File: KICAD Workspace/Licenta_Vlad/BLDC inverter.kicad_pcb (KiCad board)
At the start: 2 copper layers, 130.8 x 107.7 mm, 103 parts, among them J1 Conn_01x03, J2 Conn_01x02, J3 Conn_01x03, J4 Conn_01x02, J5 Conn_01x03, J6 Conn_01x03, Q1 BC547, Q2 IRF9530, U1 IR2101, U10 LP2950-3.3_TO92, U2 IR2101, U3 IR2101, U4 L7805, U5 LM2576HVT-12, U6 LM2576HVT-12, U7 ACS754, U8 LM393, U9 LM393

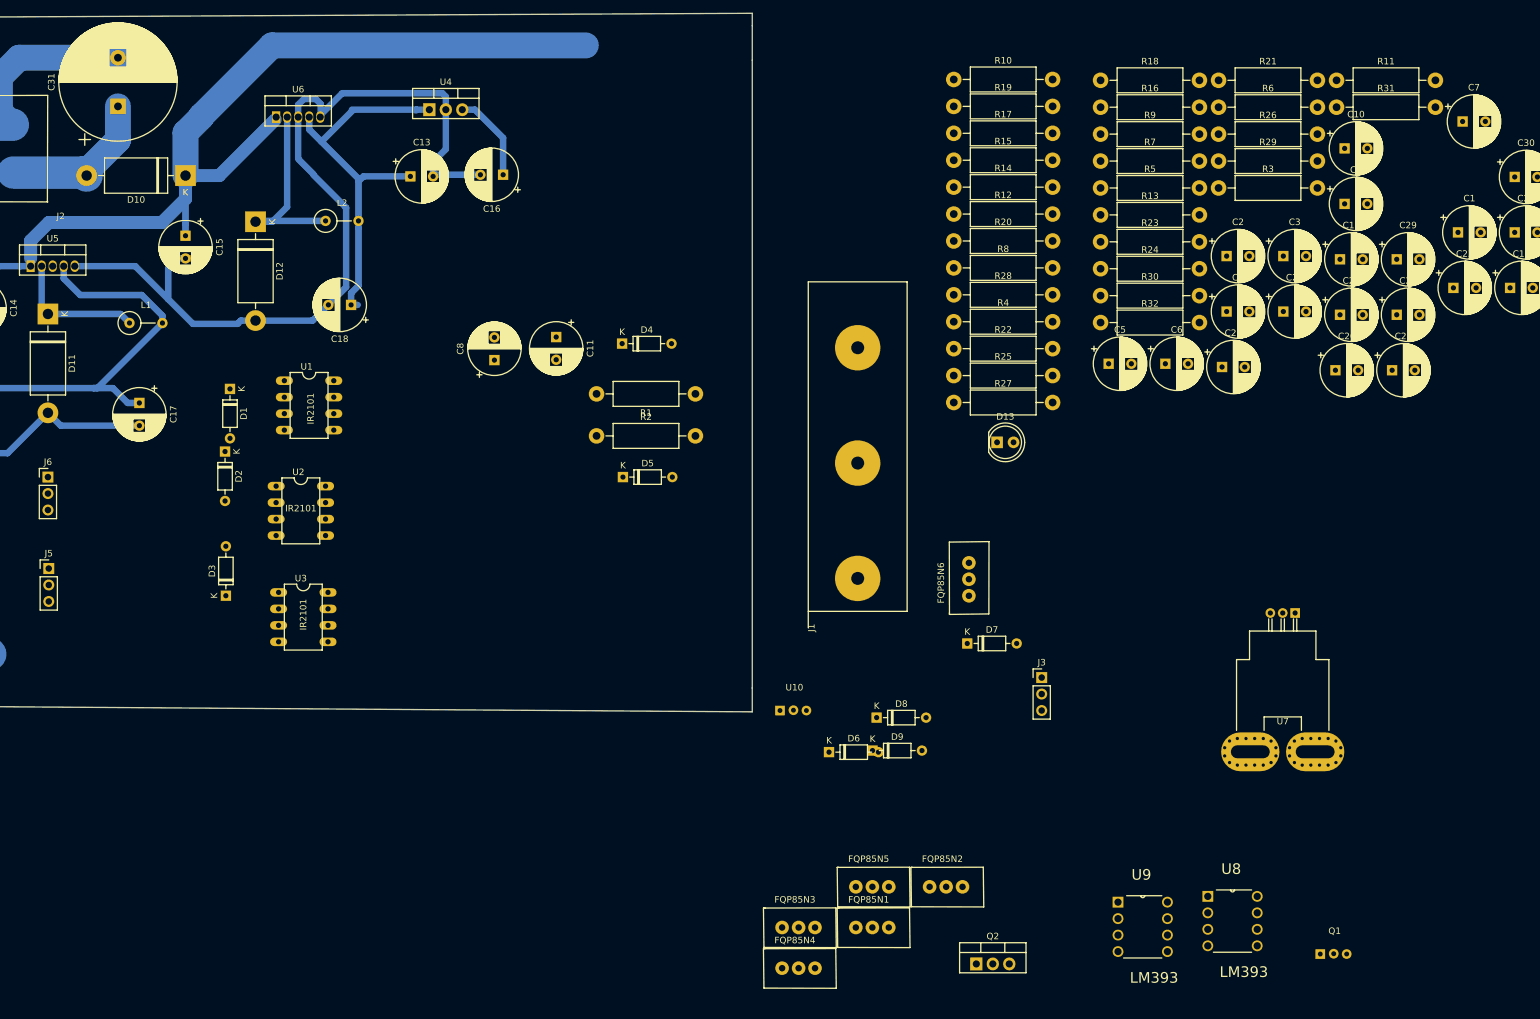
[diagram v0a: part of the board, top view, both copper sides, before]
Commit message: PCB version 1 after big big failure .......................
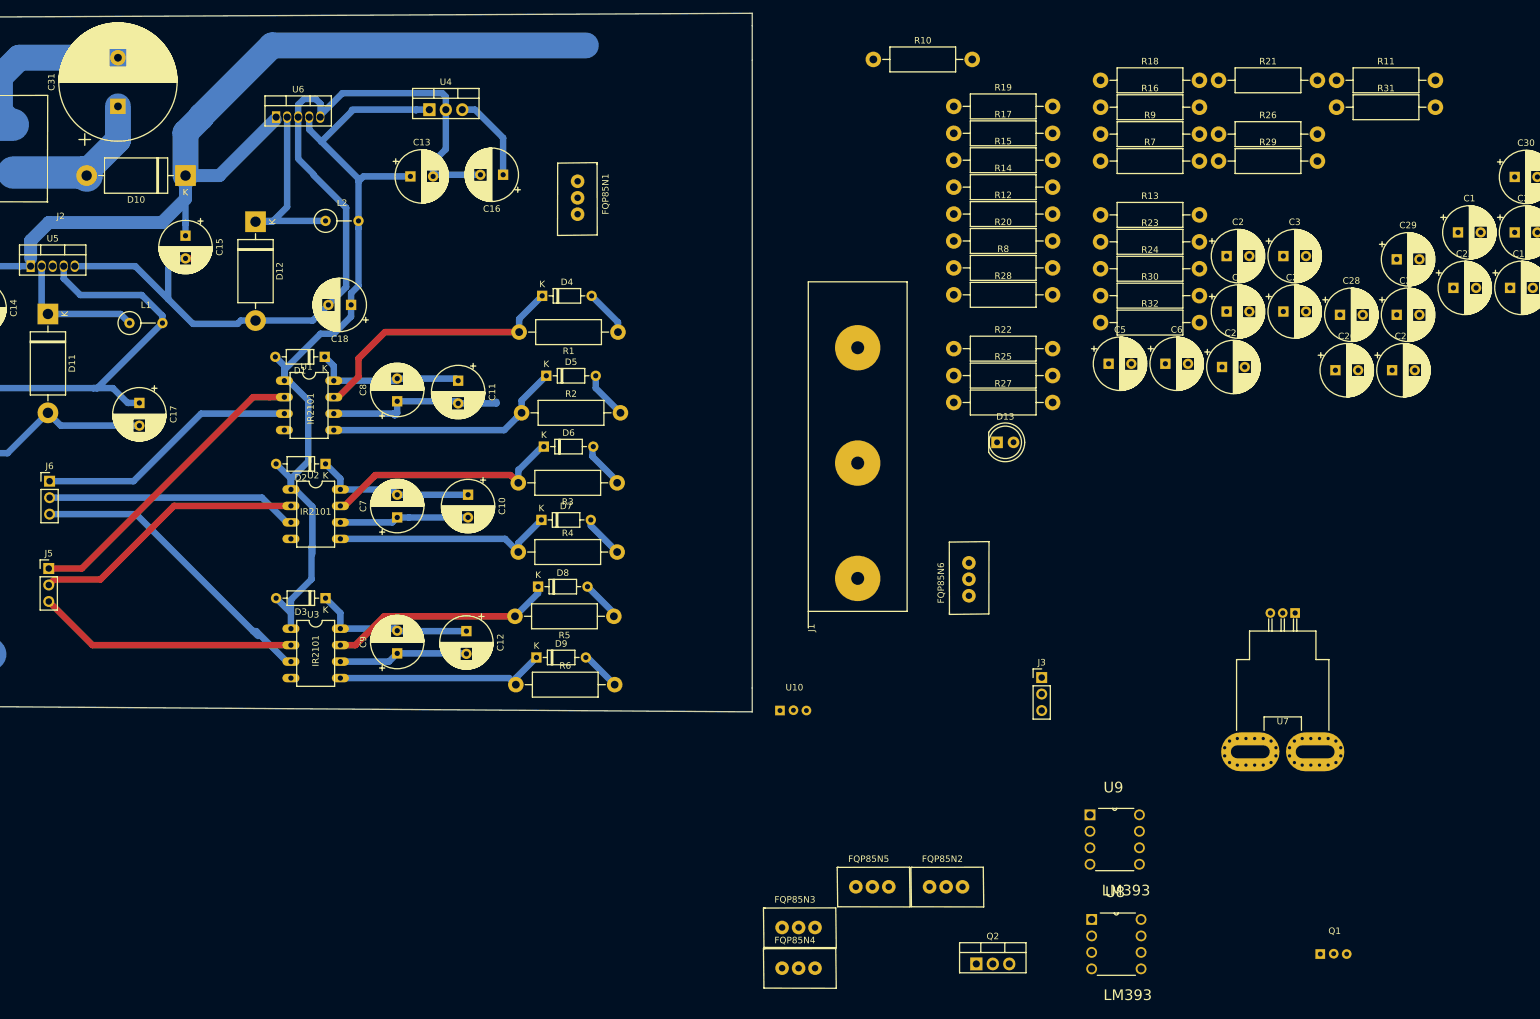
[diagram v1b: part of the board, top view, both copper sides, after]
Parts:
- moved C7 175.2 mm to (97.5, 93.7), turned to 90 degrees
- moved C9 161.7 mm to (97.5, 114.7), turned to 90 degrees
- moved C12 146.4 mm to (108.2, 111.3), turned to 270 degrees
- moved C10 145.3 mm to (108.5, 90.2), turned to 270 degrees
- moved R6 140.2 mm to (115.8, 119.5)
- moved FQP85N1 122.1 mm to (124.8, 44.5), turned to 270 degrees
- moved R3 103.3 mm to (131.4, 88.4), turned to 180 degrees
- moved R5 100.0 mm to (130.9, 109.0), turned to 180 degrees
- moved R4 75.9 mm to (116.2, 99.1)
- moved D7 68.4 mm to (119.8, 94.1)
- moved D6 64.4 mm to (120.1, 82.8)
- moved D8 56.0 mm to (119.3, 104.4)
- moved D9 53.8 mm to (119.0, 115.3)
- moved D5 19.6 mm to (120.5, 71.9)
- moved U8 18.3 mm to (212.2, 163.3)
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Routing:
- net /Sheet5CB00087/12V_Bootstrap: track 60.6 -> 134.6 mm
- net /Sheet5CB00087/LIN3: track 0.00 -> 47.7 mm
- net /Sheet5CB00087/HIN1: track 0.00 -> 47.3 mm
- net /Sheet5CB00087/HIN2: track 0.00 -> 42.4 mm
- net Net-(D4-Pad1): track 0.00 -> 41.4 mm
- net /Sheet5CB00087/LIN1: track 0.00 -> 40.5 mm
- net /Sheet5CB00087/HIN3: track 0.00 -> 40.1 mm
- net /Sheet5CB00087/LIN2: track 0.00 -> 38.8 mm
- net Net-(D5-Pad1): track 0.00 -> 38.4 mm
- net Net-(D6-Pad1): track 0.00 -> 37.0 mm
- net Net-(D8-Pad1): track 0.00 -> 34.8 mm
- net Net-(D7-Pad1): track 0.00 -> 34.7 mm
- net Net-(D9-Pad1): track 0.00 -> 33.0 mm
- net /Sheet5CB00087/PHASE_A: track 0.00 -> 27.5 mm
- net Net-(C12-Pad1): track 0.00 -> 25.2 mm
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
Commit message: Added inverter (only) pcb.
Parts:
- added J7: Conn_01x03, Connector_PinHeader_2.54mm:PinHeader_1x03_P2.54mm_Vertical, F.Cu at (35.3, 122.3)
- C1: moved to B.Cu
- moved R31 237.5 mm to (39.4, 153.8), turned to 90 degrees
- moved R29 195.4 mm to (55.6, 137.7), turned to 270 degrees
- moved C1 179.6 mm to (97.5, 124.0), turned to 90 degrees
- moved Q1 177.5 mm to (64.5, 140.0), turned to 270 degrees
- moved R32 176.7 mm to (45.8, 138.4), turned to 270 degrees
- moved C19 174.1 mm to (131.1, 164.3), turned to 270 degrees
- moved C3 167.5 mm to (97.8, 150.6), turned to 270 degrees
- moved R30 161.9 mm to (50.9, 106.3), turned to 270 degrees
- moved C2 161.7 mm to (67.8, 89.3), turned to 180 degrees
- moved 0.1uF1 158.1 mm to (125.0, 59.8), turned to 180 degrees
- moved Q2 155.1 mm to (39.4, 114.3), turned to 90 degrees
- moved R10 143.4 mm to (138.7, 162.8)
- moved C6 134.1 mm to (108.8, 150.7), turned to 270 degrees
- moved C30 133.9 mm to (136.8, 56.4), turned to 90 degrees
- moved C29 133.8 mm to (117.9, 53.6), turned to 90 degrees
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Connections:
- 0.1uF1 pad 1: +5V -> /Sheet5CB00087/3V3
- C30 pad 1: Net-(C30-Pad1) -> /Sheet5CB00087/3V3
- R15 pad 1: Net-(R15-Pad1) -> /Sheet5CB00087/PHASE_C
- R28 pad 1: Net-(C30-Pad1) -> /Sheet5CB00087/3V3
- U10 pad 1: Net-(C30-Pad1) -> /Sheet5CB00087/3V3
- U7 pad 1: +5V -> /Sheet5CB00087/3V3
- U7 pad 4: /Sheet5CB00087/CP -> GNDREF
- U7 pad 5: GNDREF -> /Sheet5CB00087/CP
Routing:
- net GNDREF: track 303.7 -> 1025.1 mm, vias 0 -> 2
- net /Sheet5CB00087/CP: track 0.00 -> 342.3 mm
- net /Sheet5CB00087/V_BAT2+: track 141.9 -> 348.5 mm
- net /Sheet5CB00087/5V: track 13.8 -> 184.4 mm
- net /Sheet5CB00087/3V3: track 0.00 -> 167.7 mm
- net /Sheet5CB00087/PHASE_B: track 20.0 -> 179.5 mm
- net /Sheet5CB00087/PHASE_A: track 27.5 -> 186.4 mm
- net /Sheet5CB00087/BEMF_C: track 0.00 -> 157.6 mm
- net /Sheet5CB00087/PHASE_C: track 20.0 -> 177.2 mm
- net /Sheet5CB00087/BEMF_B: track 0.00 -> 142.2 mm
- net /Sheet5CB00087/CURRENT_SENSOR: track 0.00 -> 132.6 mm
- net /Sheet5CB00087/EXTIB: track 0.00 -> 129.3 mm
- net /Sheet5CB00087/BEMF_A: track 0.00 -> 124.3 mm
- net /Sheet5CB00087/EXTIC: track 0.00 -> 123.5 mm
- net /Sheet5CB00087/BEMF_REF: track 0.00 -> 114.0 mm
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- added copper zone on B.Cu, net GNDREF
- added copper zone on F.Cu, net GNDREF
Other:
- board size 130.8 x 107.7 mm -> 259.7 x 159.5 mm
- board text added: "BACIU VLAD EUSEBIU"
- board text added: "SENSORLESS MOTOR CONTROLLER"
